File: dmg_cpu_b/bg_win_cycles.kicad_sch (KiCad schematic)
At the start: 96 parts

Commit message: Changes made on review.
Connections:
- net RESET_VIDEO2 renamed PPU_RESET2
- net ~{RESET_VIDEO} renamed ~{PPU_RESET}
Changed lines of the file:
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@@
     (stroke (width 0) (type default) (color 0 0 0 0))
   )
-  (wire (pts (xy 302.26 133.985) (xy 304.8 133.985))
+  (wire (pts (xy 291.465 133.985) (xy 304.8 133.985))
     (stroke (width 0) (type default) (color 0 0 0 0))
   )
@@
     (effects (font (size 1.27 1.27)) (justify left bottom))
   )
-  (label "~{RESET_VIDEO}" (at 50.165 192.405 0)
+  (label "~{PPU_RESET}" (at 50.165 192.405 0)
     (effects (font (size 1.27 1.27)) (justify left bottom))
   )
@@
     (effects (font (size 1.27 1.27)) (justify right bottom))
   )
-  (label "~{RESET_VIDEO}" (at 21.59 140.97 0)
+  (label "~{PPU_RESET}" (at 21.59 140.97 0)
     (effects (font (size 1.27 1.27)) (justify left bottom))
   )
@@
     (effects (font (size 1.27 1.27)) (justify right bottom))
   )
+  (label "~{PPU_RESET}" (at 291.465 133.985 0)
+    (effects (font (size 1.27 1.27)) (justify left bottom))
+  )
   (label "TOMU" (at 107.95 264.795 180)
     (effects (font (size 1.27 1.27)) (justify right bottom))
@@
     (effects (font (size 1.27 1.27)) (justify left bottom))
   )
-  (label "~{RESET_VIDEO}" (at 46.355 250.825 0)
+  (label "~{PPU_RESET}" (at 46.355 250.825 0)
     (effects (font (size 1.27 1.27)) (justify left bottom))
   )
@@
     (effects (font (size 1.27 1.27)) (justify left bottom))
   )
-  (label "~{RESET_VIDEO}" (at 61.595 154.305 0)
+  (label "~{PPU_RESET}" (at 61.595 154.305 0)
     (effects (font (size 1.27 1.27)) (justify left bottom))
   )
@@
     (effects (font (size 1.27 1.27)) (justify left))
   )
-  (hierarchical_label "RESET_VIDEO2" (shape input) (at 39.37 267.335 180)
+  (hierarchical_label "PPU_RESET2" (shape input) (at 39.37 267.335 180)
     (effects (font (size 1.27 1.27)) (justify right))
   )
@@
     (effects (font (size 1.27 1.27)) (justify right))
   )
-  (hierarchical_label "~{RESET_VIDEO}" (shape input) (at 302.26 133.985 180)
-    (effects (font (size 1.27 1.27)) (justify right))
-  )
+  (hierarchical_label "~{PPU_RESET}" (shape input) (at 291.465 133.985 180)
+    (effects (font (size 1.27 1.27)) (justify right))
+  )

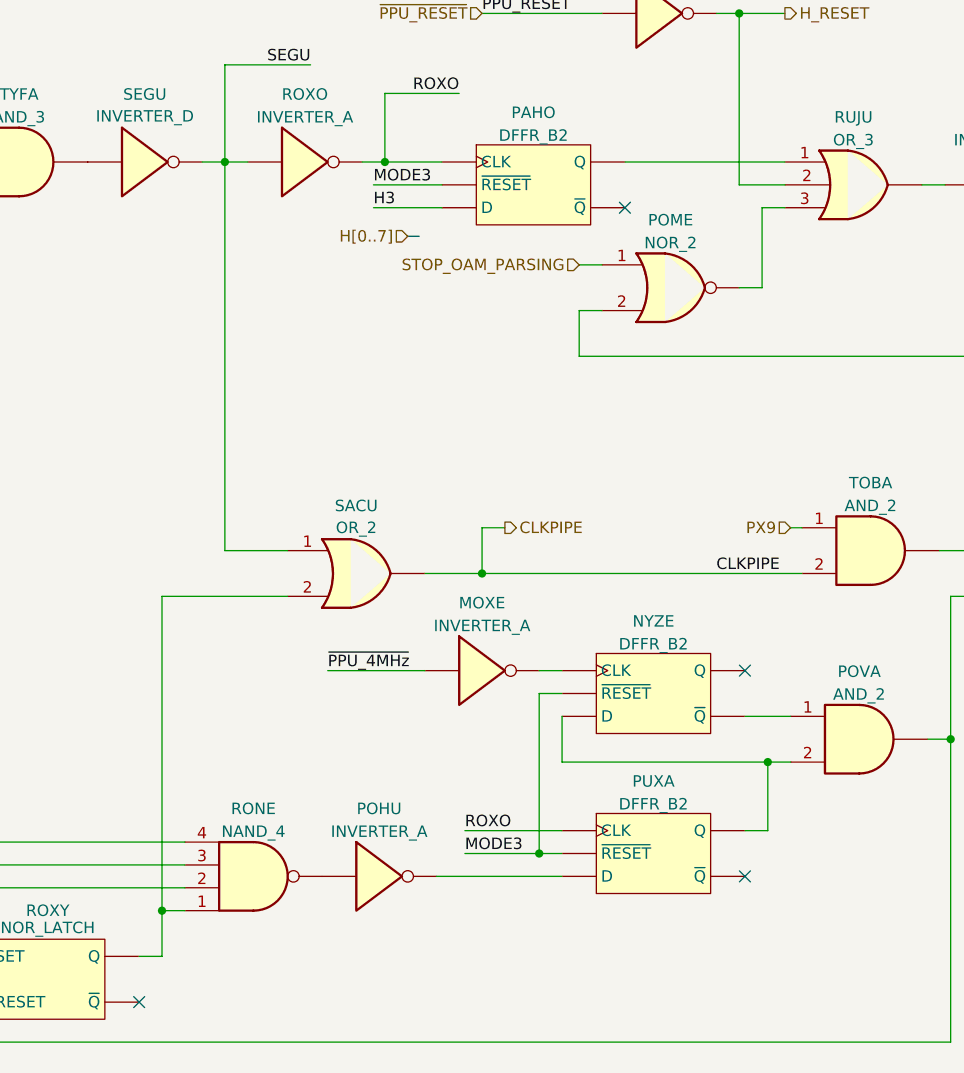
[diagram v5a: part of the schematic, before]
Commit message: Sprite Y comparator changes made from review.
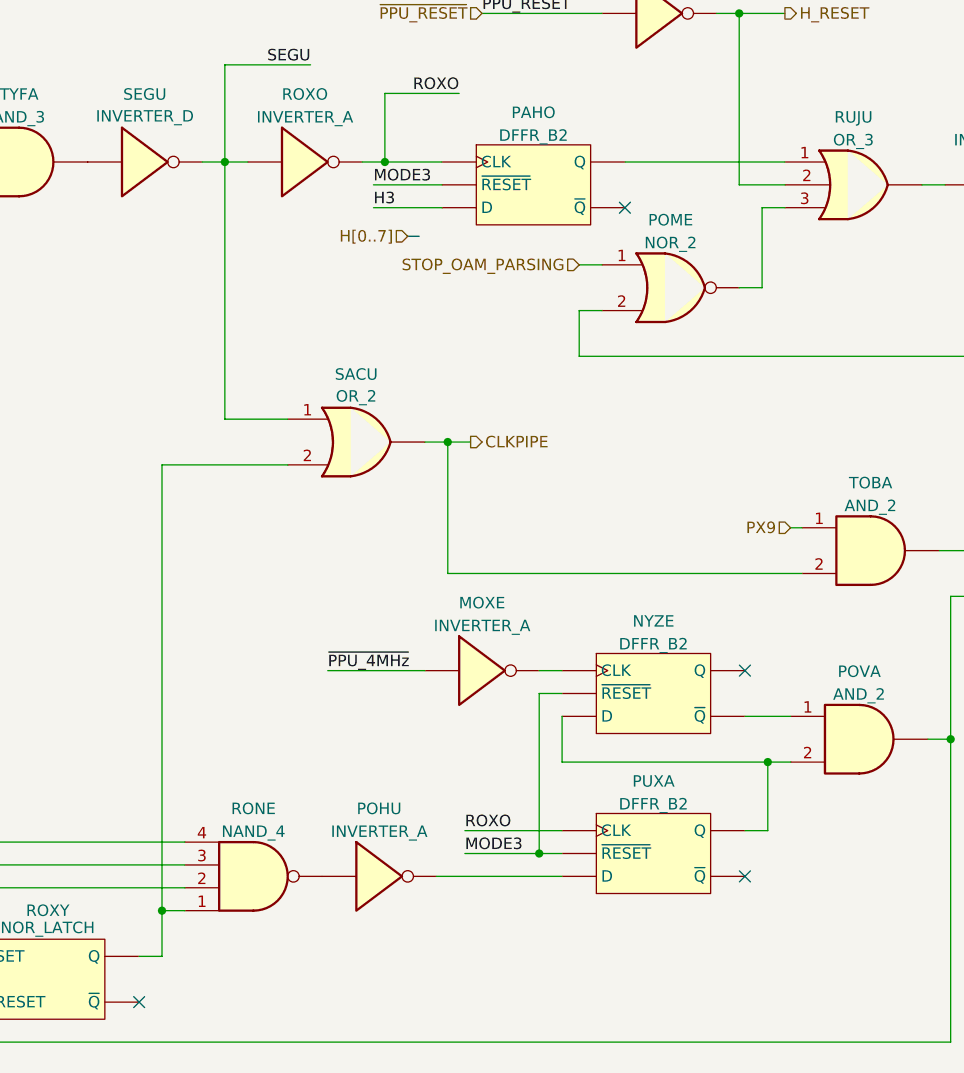
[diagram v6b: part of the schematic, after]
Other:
- moved on the sheet: SACU
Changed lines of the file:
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@@
   (junction (at 133.35 81.28) (diameter 0) (color 0 0 0 0)
   )
-  (junction (at 291.465 196.215) (diameter 0) (color 0 0 0 0)
+  (junction (at 287.655 181.61) (diameter 0) (color 0 0 0 0)
   )
   (junction (at 86.995 24.13) (diameter 0) (color 0 0 0 0)
@@
     (stroke (width 0) (type default) (color 0 0 0 0))
   )
-  (wire (pts (xy 294.005 191.135) (xy 291.465 191.135))
-    (stroke (width 0) (type default) (color 0 0 0 0))
-  )
   (wire (pts (xy 186.69 255.905) (xy 186.69 260.35))
     (stroke (width 0) (type default) (color 0 0 0 0))
@@
     (stroke (width 0) (type default) (color 0 0 0 0))
   )
-  (wire (pts (xy 255.905 198.755) (xy 269.875 198.755))
+  (wire (pts (xy 255.905 184.15) (xy 269.875 184.15))
     (stroke (width 0) (type default) (color 0 0 0 0))
   )
@@
     (stroke (width 0) (type default) (color 0 0 0 0))
   )
-  (wire (pts (xy 255.905 198.755) (xy 255.905 233.68))
+  (wire (pts (xy 287.655 181.61) (xy 290.195 181.61))
+    (stroke (width 0) (type default) (color 0 0 0 0))
+  )
+  (wire (pts (xy 255.905 184.15) (xy 255.905 233.68))
     (stroke (width 0) (type default) (color 0 0 0 0))
   )
@@
     (stroke (width 0) (type default) (color 0 0 0 0))
   )
-  (wire (pts (xy 285.115 196.215) (xy 291.465 196.215))
+  (wire (pts (xy 285.115 181.61) (xy 287.655 181.61))
     (stroke (width 0) (type default) (color 0 0 0 0))
   )
@@
     (stroke (width 0) (type default) (color 0 0 0 0))
   )
-  (wire (pts (xy 262.89 150.495) (xy 262.89 193.675))
+  (wire (pts (xy 262.89 150.495) (xy 262.89 179.07))
     (stroke (width 0) (type default) (color 0 0 0 0))
   )
@@
     (stroke (width 0) (type default) (color 0 0 0 0))
   )
-  (wire (pts (xy 291.465 196.215) (xy 327.025 196.215))
+  (wire (pts (xy 287.655 196.215) (xy 327.025 196.215))
     (stroke (width 0) (type default) (color 0 0 0 0))
   )
@@
     (stroke (width 0) (type default) (color 0 0 0 0))
   )
-  (wire (pts (xy 291.465 191.135) (xy 291.465 196.215))
+  (wire (pts (xy 287.655 181.61) (xy 287.655 196.215))
     (stroke (width 0) (type default) (color 0 0 0 0))
   )
@@
     (stroke (width 0) (type default) (color 0 0 0 0))
   )
-  (wire (pts (xy 262.89 193.675) (xy 269.875 193.675))
+  (wire (pts (xy 262.89 179.07) (xy 269.875 179.07))
     (stroke (width 0) (type default) (color 0 0 0 0))
   )
@@
     (effects (font (size 1.27 1.27)) (justify left bottom))
   )
-  (label "CLKPIPE" (at 317.5 196.215 0)
-    (effects (font (size 1.27 1.27)) (justify left bottom))
-  )
   (label "~{PPU_4MHz}" (at 100.33 58.42 0)
     (effects (font (size 1.27 1.27)) (justify left bottom))
@@
     (effects (font (size 1.27 1.27)) (justify right))
   )
-  (hierarchical_label "CLKPIPE" (shape output) (at 294.005 191.135 0)
+  (hierarchical_label "CLKPIPE" (shape output) (at 290.195 181.61 0)
     (effects (font (size 1.27 1.27)) (justify left))
   )
@@
     (pin "2")
   )
-  (symbol (lib_id "DMG_CPU_Cells:OR_2") (at 277.495 196.215 0) (unit 1)
+  (symbol (lib_id "DMG_CPU_Cells:OR_2") (at 277.495 181.61 0) (unit 1)
     (in_bom yes) (on_board yes)
-    (property "Reference" "SACU" (id 0) (at 277.4948 188.7052 0))
-    (property "Value" "OR_2" (id 1) (at 277.495 191.135 0))
-    (property "Footprint" "" (id 2) (at 277.241 196.215 0)
-      (effects (font (size 1.27 1.27)) hide)
-    )
-    (property "Datasheet" "http://iceboy.a-singer.de/doc/dmg_cells.html#or2" (id 3) (at 277.495 203.835 0)
-      (effects (font (size 1.27 1.27)) hide)
-    )
+    (property "Reference" "SACU" (id 0) (at 277.4948 174.1002 0))
+    (property "Value" "OR_2" (id 1) (at 277.495 176.53 0))
+    (property "Footprint" "" (id 2) (at 277.241 181.61 0)
+      (effects (font (size 1.27 1.27)) hide)
+    )
+    (property "Datasheet" "http://iceboy.a-singer.de/doc/dmg_cells.html#or2" (id 3) (at 277.495 189.23 0)
+      (effects (font (size 1.27 1.27)) hide)
+    )

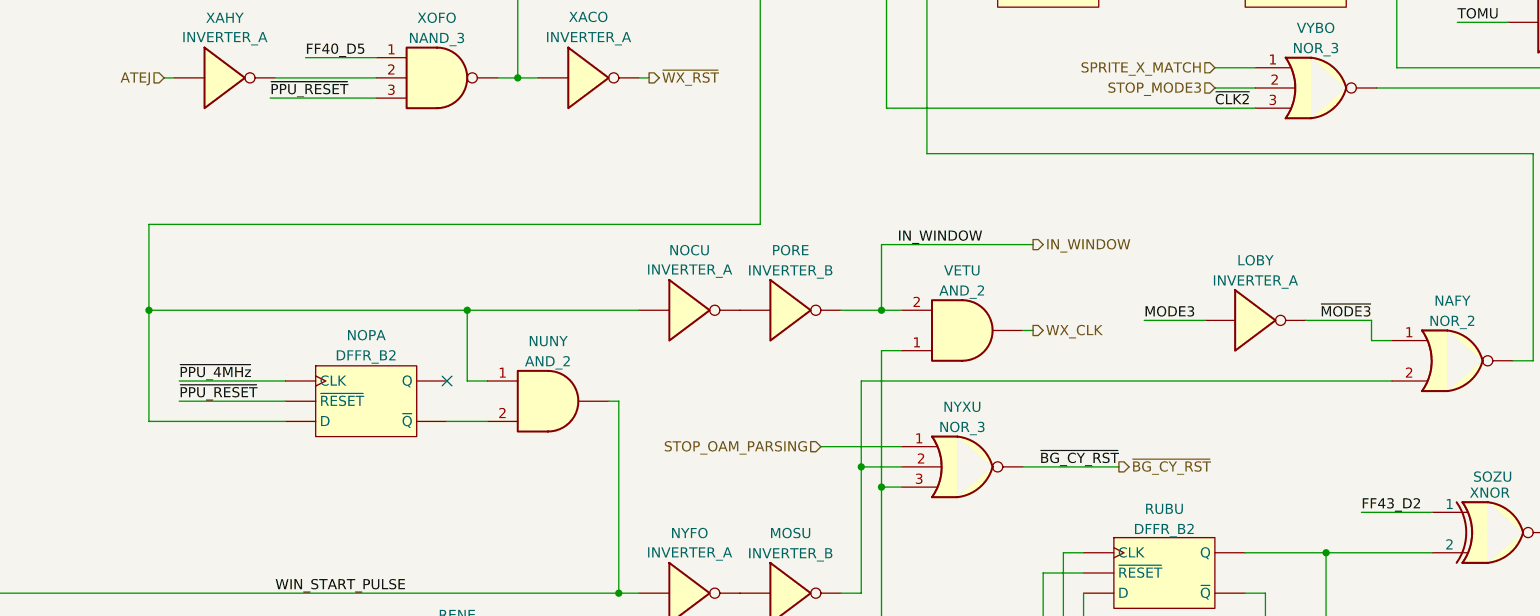
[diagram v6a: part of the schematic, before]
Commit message: Elements from sptite control sheet moved to lcd sheet.
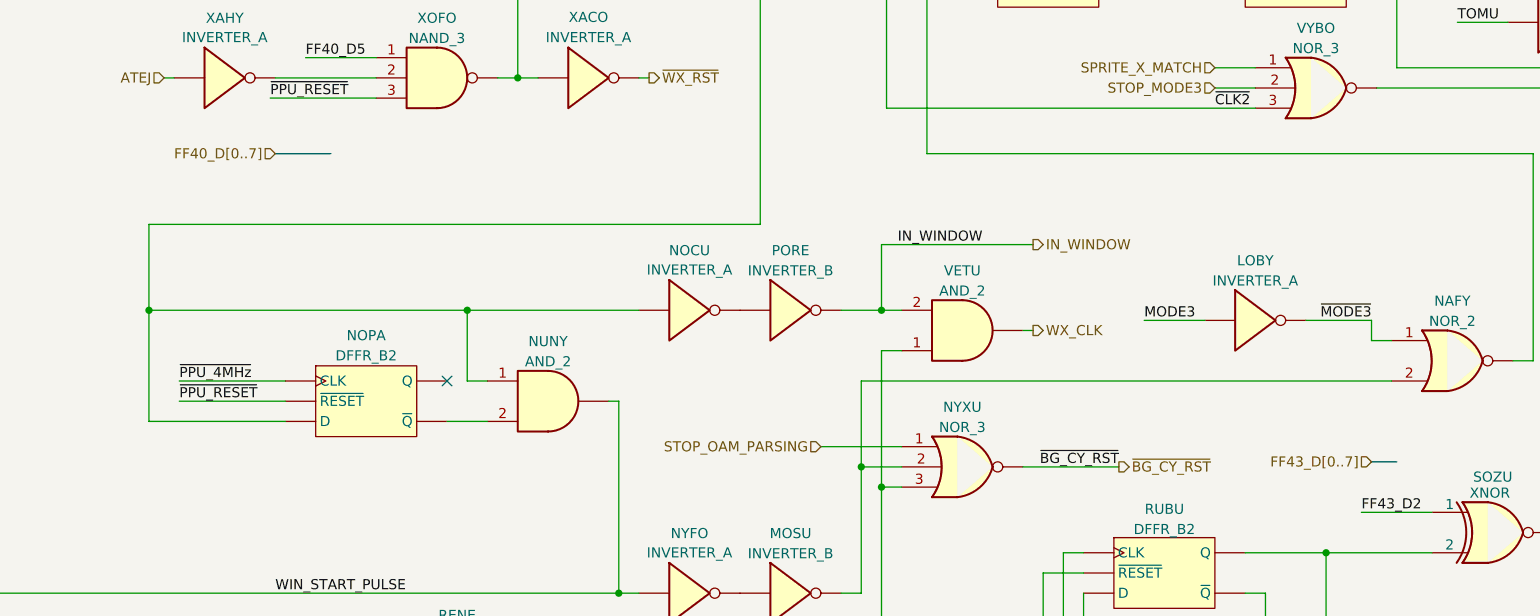
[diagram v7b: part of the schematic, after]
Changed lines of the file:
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@@
+    (stroke (width 0) (type default) (color 0 0 0 0))
+  )
+  (bus (pts (xy 203.2 200.025) (xy 200.025 200.025))
     (stroke (width 0) (type default) (color 0 0 0 0))
   )
@@
   )
   (wire (pts (xy 207.645 73.025) (xy 210.185 73.025))
+    (stroke (width 0) (type default) (color 0 0 0 0))
+  )
+  (bus (pts (xy 62.23 161.29) (xy 69.215 161.29))
     (stroke (width 0) (type default) (color 0 0 0 0))
   )
@@
     (effects (font (size 1.27 1.27)) (justify left))
   )
+  (hierarchical_label "FF43_D[0..7]" (shape input) (at 200.025 200.025 180)
+    (effects (font (size 1.27 1.27)) (justify right))
+  )
   (hierarchical_label "STOP_MODE3" (shape input) (at 180.34 153.035 180)
     (effects (font (size 1.27 1.27)) (justify right))
@@
     (effects (font (size 1.27 1.27)) (justify right))
   )
+  (hierarchical_label "FF40_D[0..7]" (shape input) (at 62.23 161.29 180)
+    (effects (font (size 1.27 1.27)) (justify right))
+  )
